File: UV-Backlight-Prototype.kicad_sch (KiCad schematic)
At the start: 25 parts

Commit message: Connector
Connector Schematic update
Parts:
- added J?: Conn_02x08_Odd_Even, symbol Connector_Generic:Conn_02x08_Odd_Even
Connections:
- net GND-LED1: now also J?.1 (Pin_1)
- net GND-LED2: now also J?.7 (Pin_7)
- net GND-LED3: now also J?.13 (Pin_13)
- net T1-In: now also J?.4 (Pin_4)
- net T1-Out: now also J?.3 (Pin_3)
- net T2-In: now also J?.6 (Pin_6)
- net T2-Out: now also J?.5 (Pin_5)
- net T3-In: now also J?.10 (Pin_10)
- net T3-Out: now also J?.9 (Pin_9)
- net T4-In: now also J?.12 (Pin_12)
- net T4-Out: now also J?.11 (Pin_11)
- net VCC-LED1: now also J?.2 (Pin_2)
- net VCC-LED2: now also J?.8 (Pin_8)
- net VCC-LED3: now also J?.14 (Pin_14)
- no-connect marks 0 -> 2
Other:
- note added: "Connector"
- note added: "LED Array"
- note added: "Thermsistors"
- moved on the sheet: TH?

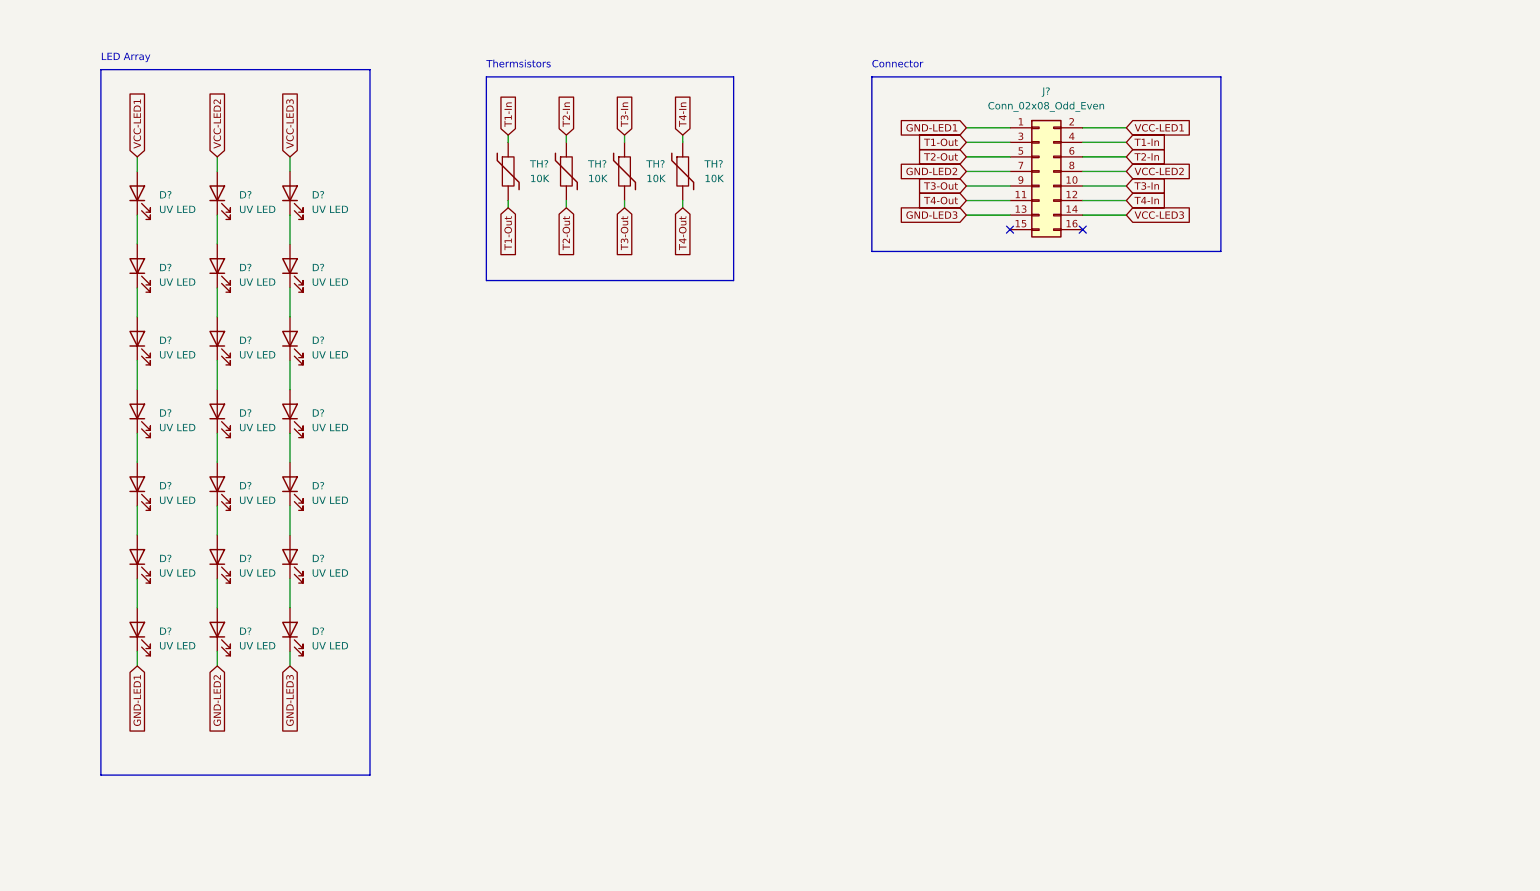
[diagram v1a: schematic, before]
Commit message: Update UV-Backlight-Prototype.kicad_sch
Added Test points to each LED NET
Added 0 ohm jumper for matrix config
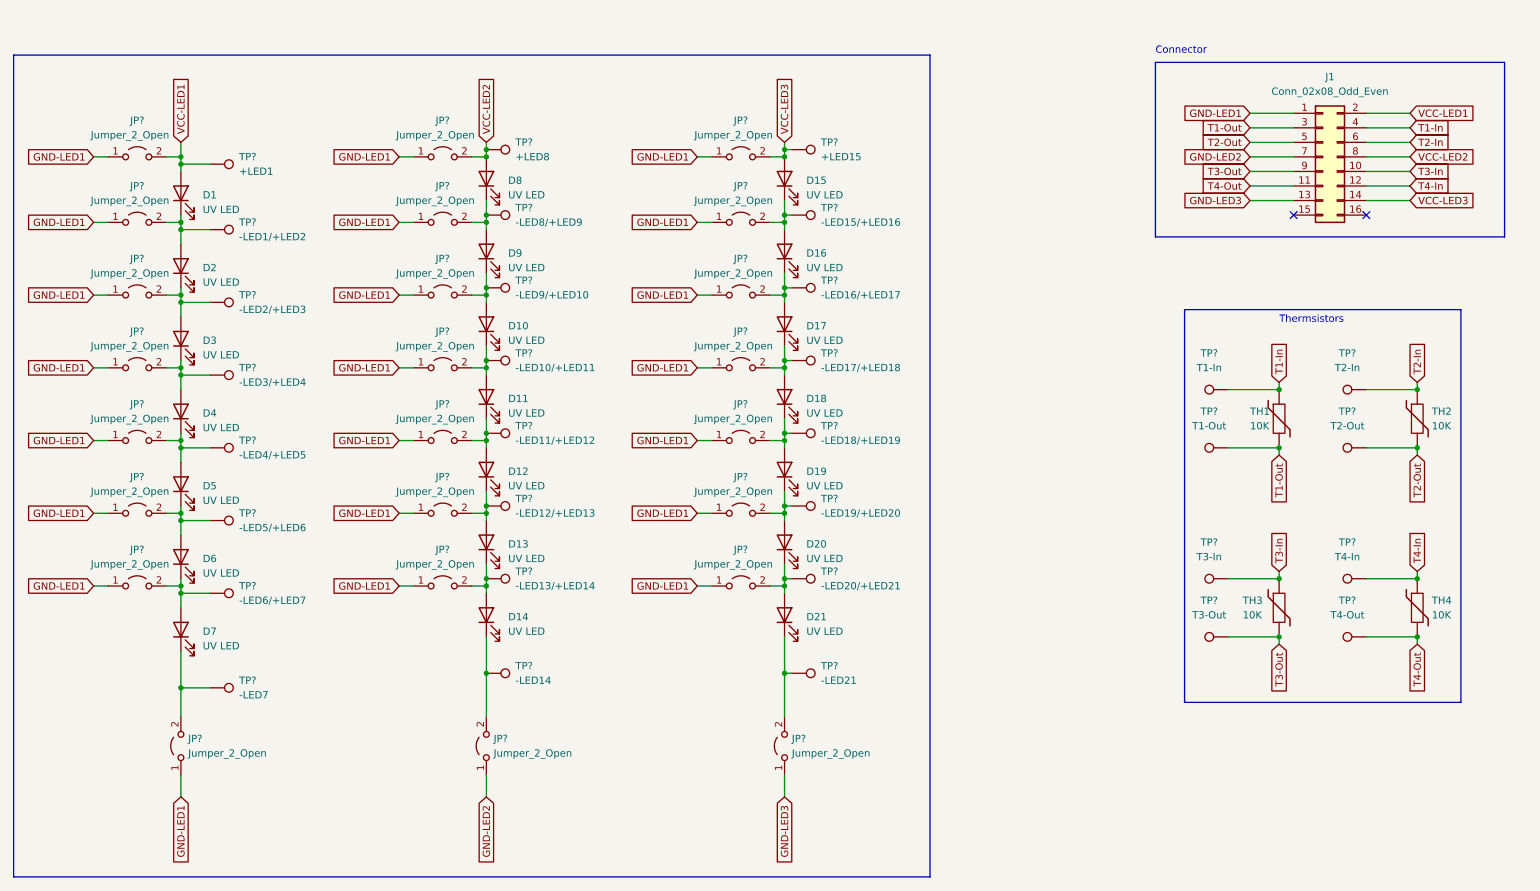
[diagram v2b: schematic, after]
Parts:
- added JP? (x24): Jumper_2_Open, symbol Jumper:Jumper_2_Open
- added TP?: -LED12/+LED13, TestPoint:TestPoint_Keystone_5000-5004_Miniature, symbol Connector:TestPoint
- added TP?: -LED3/+LED4, TestPoint:TestPoint_Keystone_5000-5004_Miniature, symbol Connector:TestPoint
- added TP?: -LED21, TestPoint:TestPoint_Keystone_5000-5004_Miniature, symbol Connector:TestPoint
- added TP?: -LED6/+LED7, TestPoint:TestPoint_Keystone_5000-5004_Miniature, symbol Connector:TestPoint
- added TP?: T1-Out, TestPoint:TestPoint_Keystone_5000-5004_Miniature, symbol Connector:TestPoint
- added TP?: -LED2/+LED3, TestPoint:TestPoint_Keystone_5000-5004_Miniature, symbol Connector:TestPoint
- added TP?: -LED10/+LED11, TestPoint:TestPoint_Keystone_5000-5004_Miniature, symbol Connector:TestPoint
- added TP?: -LED4/+LED5, TestPoint:TestPoint_Keystone_5000-5004_Miniature, symbol Connector:TestPoint
- added TP?: -LED9/+LED10, TestPoint:TestPoint_Keystone_5000-5004_Miniature, symbol Connector:TestPoint
- added TP?: -LED14, TestPoint:TestPoint_Keystone_5000-5004_Miniature, symbol Connector:TestPoint
- added TP?: +LED8, TestPoint:TestPoint_Keystone_5000-5004_Miniature, symbol Connector:TestPoint
- added TP?: -LED17/+LED18, TestPoint:TestPoint_Keystone_5000-5004_Miniature, symbol Connector:TestPoint
- added TP?: -LED13/+LED14, TestPoint:TestPoint_Keystone_5000-5004_Miniature, symbol Connector:TestPoint
- added TP?: -LED16/+LED17, TestPoint:TestPoint_Keystone_5000-5004_Miniature, symbol Connector:TestPoint
- added TP?: -LED1/+LED2, TestPoint:TestPoint_Keystone_5000-5004_Miniature, symbol Connector:TestPoint
- added TP?: -LED11/+LED12, TestPoint:TestPoint_Keystone_5000-5004_Miniature, symbol Connector:TestPoint
- added TP?: -LED19/+LED20, TestPoint:TestPoint_Keystone_5000-5004_Miniature, symbol Connector:TestPoint
- added TP?: T2-Out, TestPoint:TestPoint_Keystone_5000-5004_Miniature, symbol Connector:TestPoint
- added TP?: -LED7, TestPoint:TestPoint_Keystone_5000-5004_Miniature, symbol Connector:TestPoint
- added TP?: -LED15/+LED16, TestPoint:TestPoint_Keystone_5000-5004_Miniature, symbol Connector:TestPoint
- added TP?: T2-In, TestPoint:TestPoint_Keystone_5000-5004_Miniature, symbol Connector:TestPoint
- added TP?: -LED5/+LED6, TestPoint:TestPoint_Keystone_5000-5004_Miniature, symbol Connector:TestPoint
- added TP?: -LED8/+LED9, TestPoint:TestPoint_Keystone_5000-5004_Miniature, symbol Connector:TestPoint
- added TP?: +LED1, symbol Connector:TestPoint
- added TP?: +LED15, TestPoint:TestPoint_Keystone_5000-5004_Miniature, symbol Connector:TestPoint
- added TP?: -LED20/+LED21, TestPoint:TestPoint_Keystone_5000-5004_Miniature, symbol Connector:TestPoint
- added TP?: T4-Out, TestPoint:TestPoint_Keystone_5000-5004_Miniature, symbol Connector:TestPoint
- added TP?: T3-In, TestPoint:TestPoint_Keystone_5000-5004_Miniature, symbol Connector:TestPoint
- added TP?: T1-In, TestPoint:TestPoint_Keystone_5000-5004_Miniature, symbol Connector:TestPoint
- added TP?: T3-Out, TestPoint:TestPoint_Keystone_5000-5004_Miniature, symbol Connector:TestPoint
- added TP?: T4-In, TestPoint:TestPoint_Keystone_5000-5004_Miniature, symbol Connector:TestPoint
- added TP?: -LED18/+LED19, TestPoint:TestPoint_Keystone_5000-5004_Miniature, symbol Connector:TestPoint
- J1: renamed from J?; footprint (none) -> Connector_IDC:IDC-Header_2x08_P2.54mm_Vertical
- gave numbers to parts that had none: 25
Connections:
- net GND-LED1: now also JP?.1 (A), JP?.1 (A), JP?.1 (A), JP?.1 (A), JP?.1 (A), JP?.1 (A), JP?.1 (A), JP?.1 (A), JP?.1 (A), JP?.1 (A), JP?.1 (A), JP?.1 (A), JP?.1 (A), JP?.1 (A), JP?.1 (A), JP?.1 (A), JP?.1 (A), JP?.1 (A), JP?.1 (A), JP?.1 (A), JP?.1 (A), JP?.1 (A); no longer D7.1 (K)
- net GND-LED2: now also JP?.1 (A); no longer D14.1 (K)
- net GND-LED3: now also JP?.1 (A); no longer D21.1 (K)
- net T1-In: now also TP?.1
- net T1-Out: now also TP?.1
- net T2-In: now also TP?.1
- net T2-Out: now also TP?.1
- net T3-In: now also TP?.1
- net T3-Out: now also TP?.1
- net T4-In: now also TP?.1
- net T4-Out: now also TP?.1
- net VCC-LED1: now also JP?.2 (B), TP?.1
- net VCC-LED2: now also JP?.2 (B), TP?.1
- net VCC-LED3: now also JP?.2 (B), TP?.1
- net at D10.1 (K), D11.2 (A): now also JP?.2 (B), TP?.1
- net at D10.2 (A), D9.1 (K): now also JP?.2 (B), TP?.1
- net at D16.1 (K), D17.2 (A): now also JP?.2 (B), TP?.1
- net at D15.1 (K), D16.2 (A): now also JP?.2 (B), TP?.1
- net at D12.1 (K), D13.2 (A): now also JP?.2 (B), TP?.1
- net at D11.1 (K), D12.2 (A): now also JP?.2 (B), TP?.1
- net at D8.1 (K), D9.2 (A): now also JP?.2 (B), TP?.1
- net at D2.1 (K), D3.2 (A): now also JP?.2 (B), TP?.1
- net at D1.1 (K), D2.2 (A): now also JP?.2 (B), TP?.1
- net at D20.1 (K), D21.2 (A): now also JP?.2 (B), TP?.1
- net at D6.1 (K), D7.2 (A): now also JP?.2 (B), TP?.1
- net at D5.1 (K), D6.2 (A): now also JP?.2 (B), TP?.1
- net at D19.1 (K), D20.2 (A): now also JP?.2 (B), TP?.1
- net at D18.1 (K), D19.2 (A): now also JP?.2 (B), TP?.1
- net at D4.1 (K), D5.2 (A): now also JP?.2 (B), TP?.1
- net at D3.1 (K), D4.2 (A): now also JP?.2 (B), TP?.1
- net at D17.1 (K), D18.2 (A): now also JP?.2 (B), TP?.1
- net at D13.1 (K), D14.2 (A): now also JP?.2 (B), TP?.1
- new net: D21.1 (K), JP?.2 (B), TP?.1
- new net: D14.1 (K), JP?.2 (B), TP?.1
- new net: D7.1 (K), JP?.2 (B), TP?.1
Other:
- note removed: "LED Array"
- moved on the sheet: D1, D10, D11, D12, D13, D14, D15, D16, D17, D18, D19, D2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

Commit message: Schematic
Assigned footprints
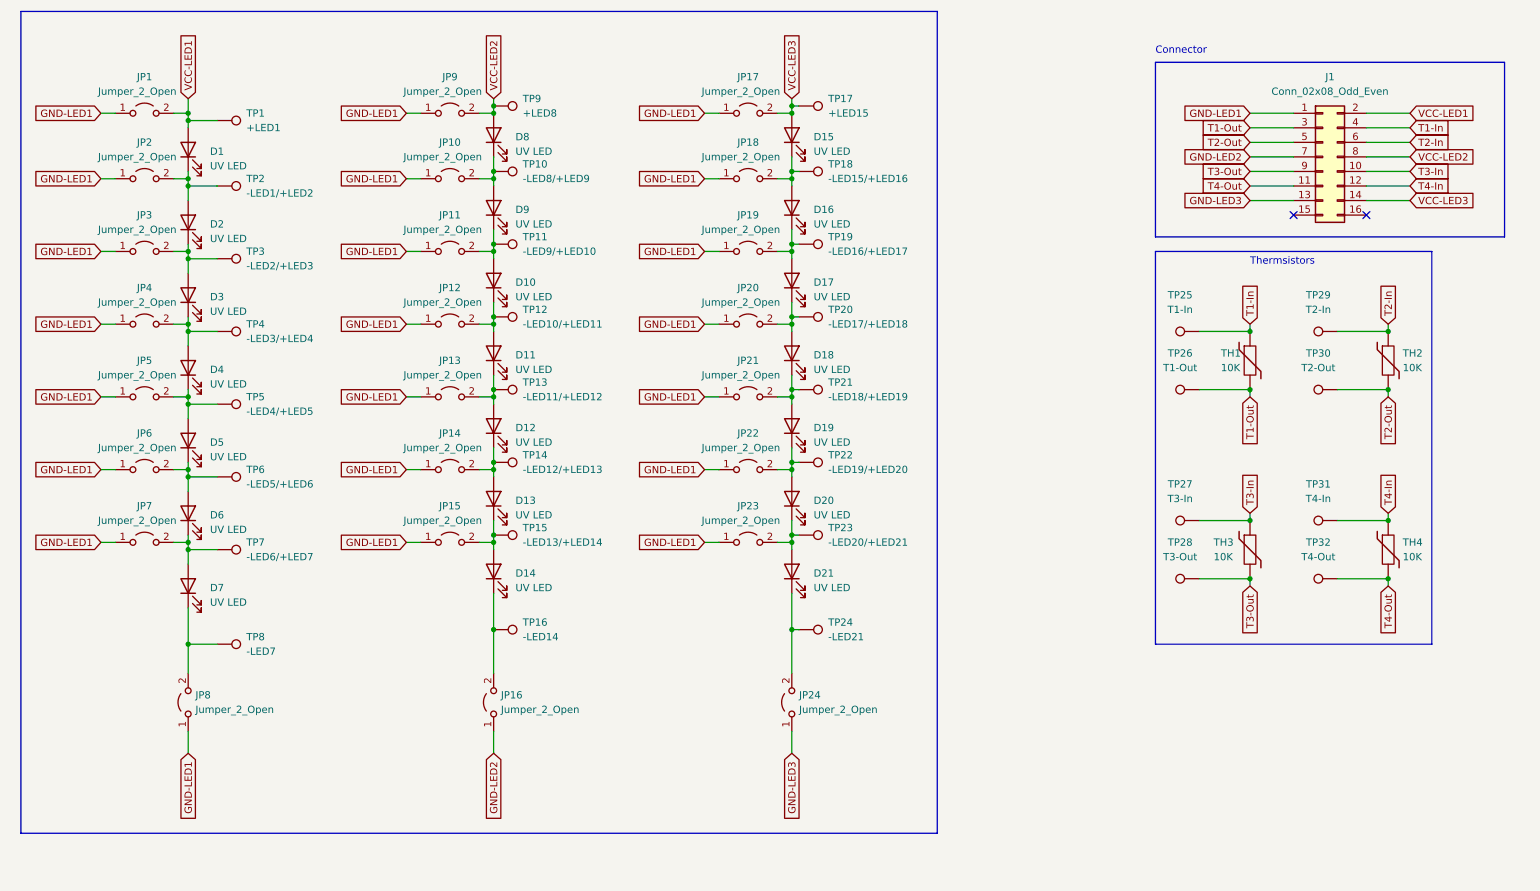
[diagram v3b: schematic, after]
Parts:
- JP1, JP10, JP11, JP12, JP13, JP14, JP15, JP17, JP18, JP19, JP2, JP20, JP21, JP22, JP23, JP3, JP4, JP5, JP6, JP7, JP9: renamed from JP?; footprint (none) -> Resistor_SMD:R_1206_3216Metric_Pad1.30x1.75mm_HandSolder
- JP16, JP24, JP8: renamed from JP?; footprint (none) -> Connector_PinHeader_2.54mm:PinHeader_1x02_P2.54mm_Vertical
- gave numbers to parts that had none: 32
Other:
- moved on the sheet: D1, D10, D11, D12, D13, D14, D15, D16, D17, D18, D19, D2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
